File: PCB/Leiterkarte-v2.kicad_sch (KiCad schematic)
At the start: 50 parts

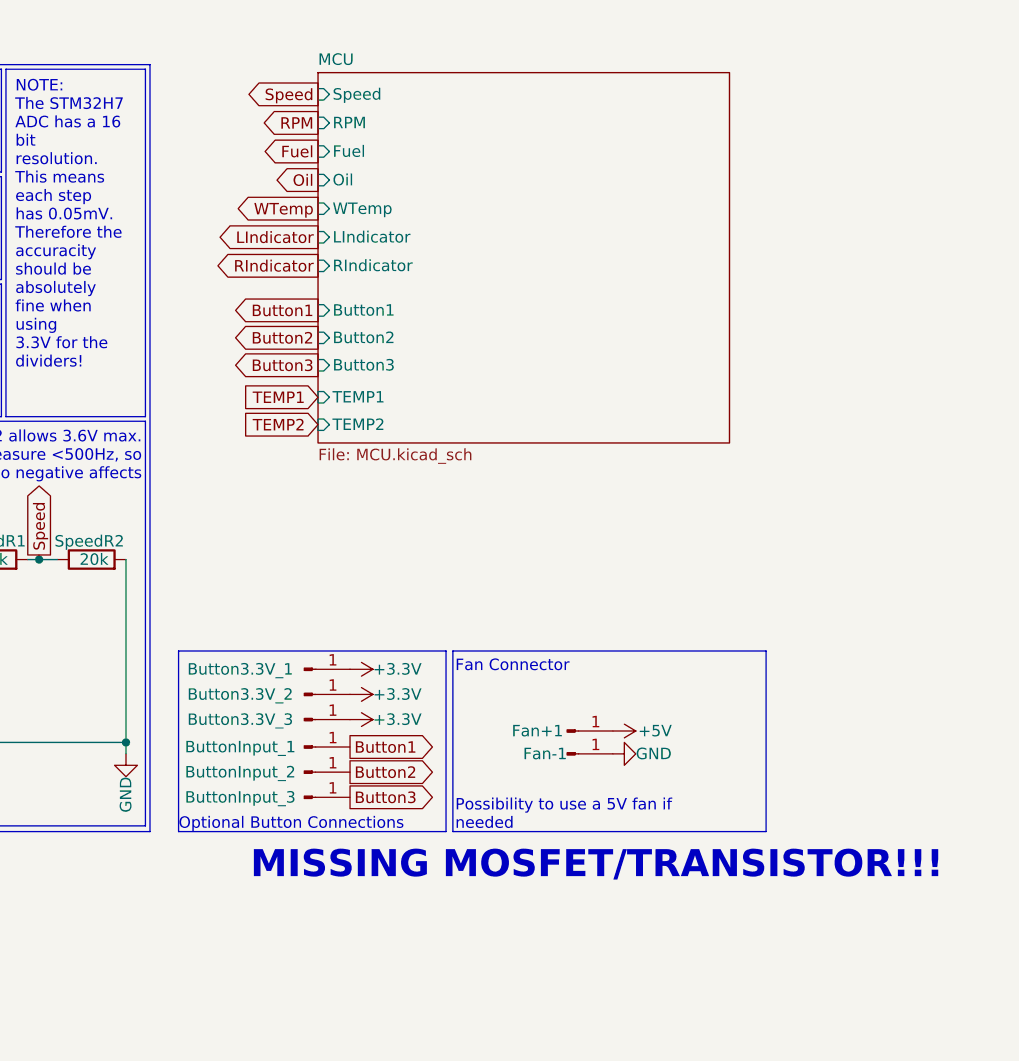
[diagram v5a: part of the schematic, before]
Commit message: Finalized circuit design; First try of PCB layout (FAILED)
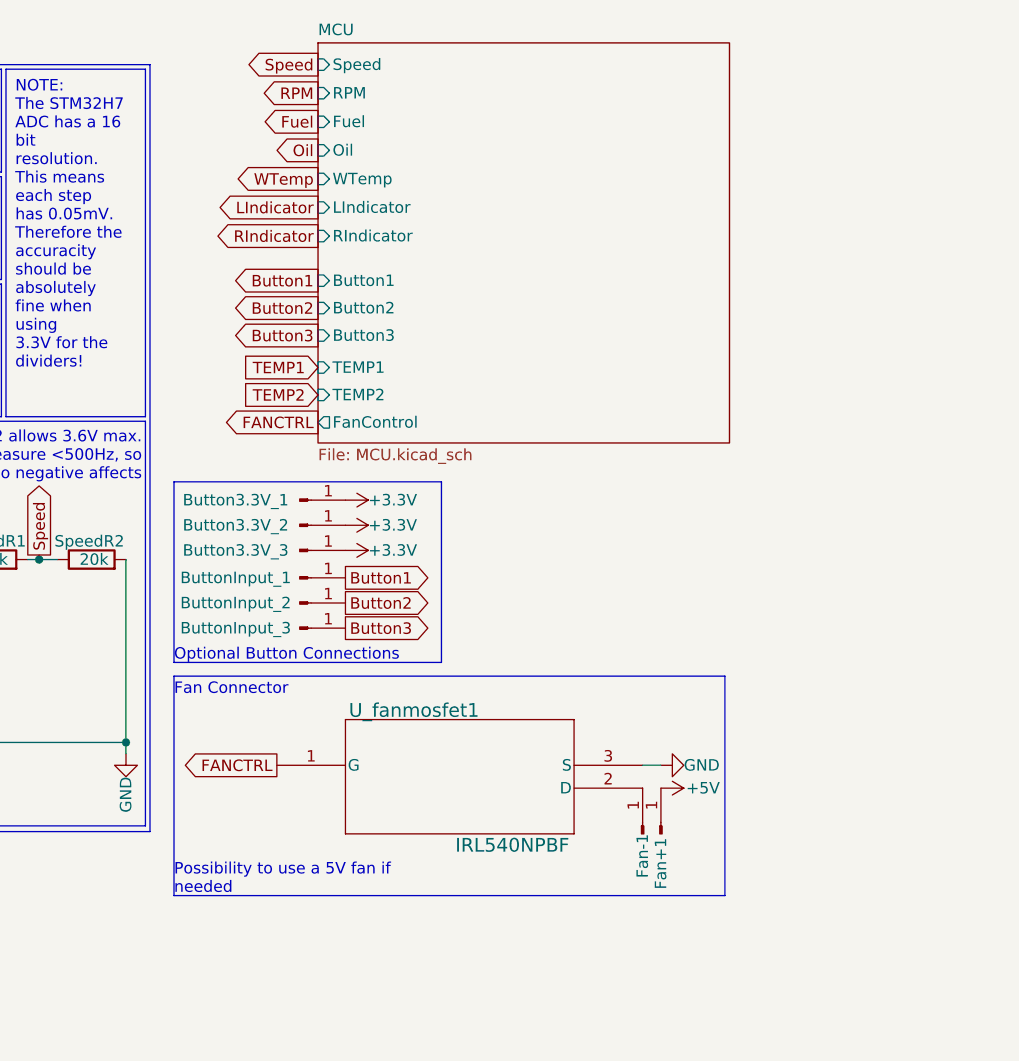
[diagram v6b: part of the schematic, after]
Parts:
- added U_fanmosfet1: IRL540NPBF, IRL540NPBF:PG-TO220-3_INF, symbol IRL540NPBF:IRL540NPBF
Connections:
- net GND: now also U_fanmosfet1.3 (S); no longer Fan-1.1 (Pin_1)
- new net: Fan-1.1 (Pin_1), U_fanmosfet1.2 (D)
- new net FANCTRL: U_fanmosfet1.1 (G)
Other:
- sheet MCU ports: added FanControl; removed none
- note removed: "MISSING MOSFET/TRANSISTOR!!!"
- moved on the sheet: Button3.3V_1, Button3.3V_2, Button3.3V_3, ButtonInput_1, ButtonInput_2, ButtonInput_3, Fan-1

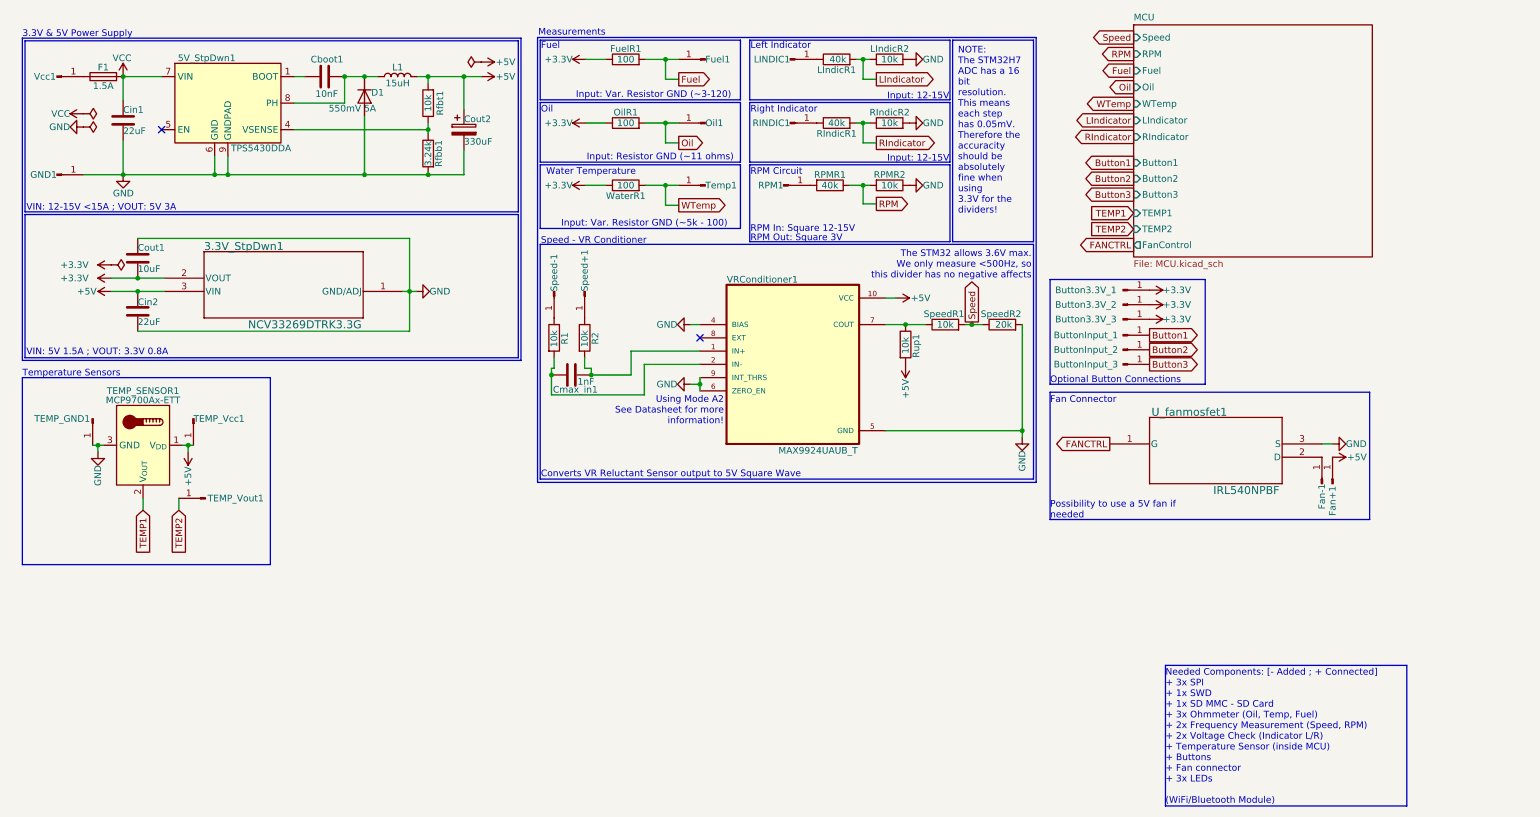
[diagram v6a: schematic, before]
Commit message: Finalized circuit design; Added PCB layout
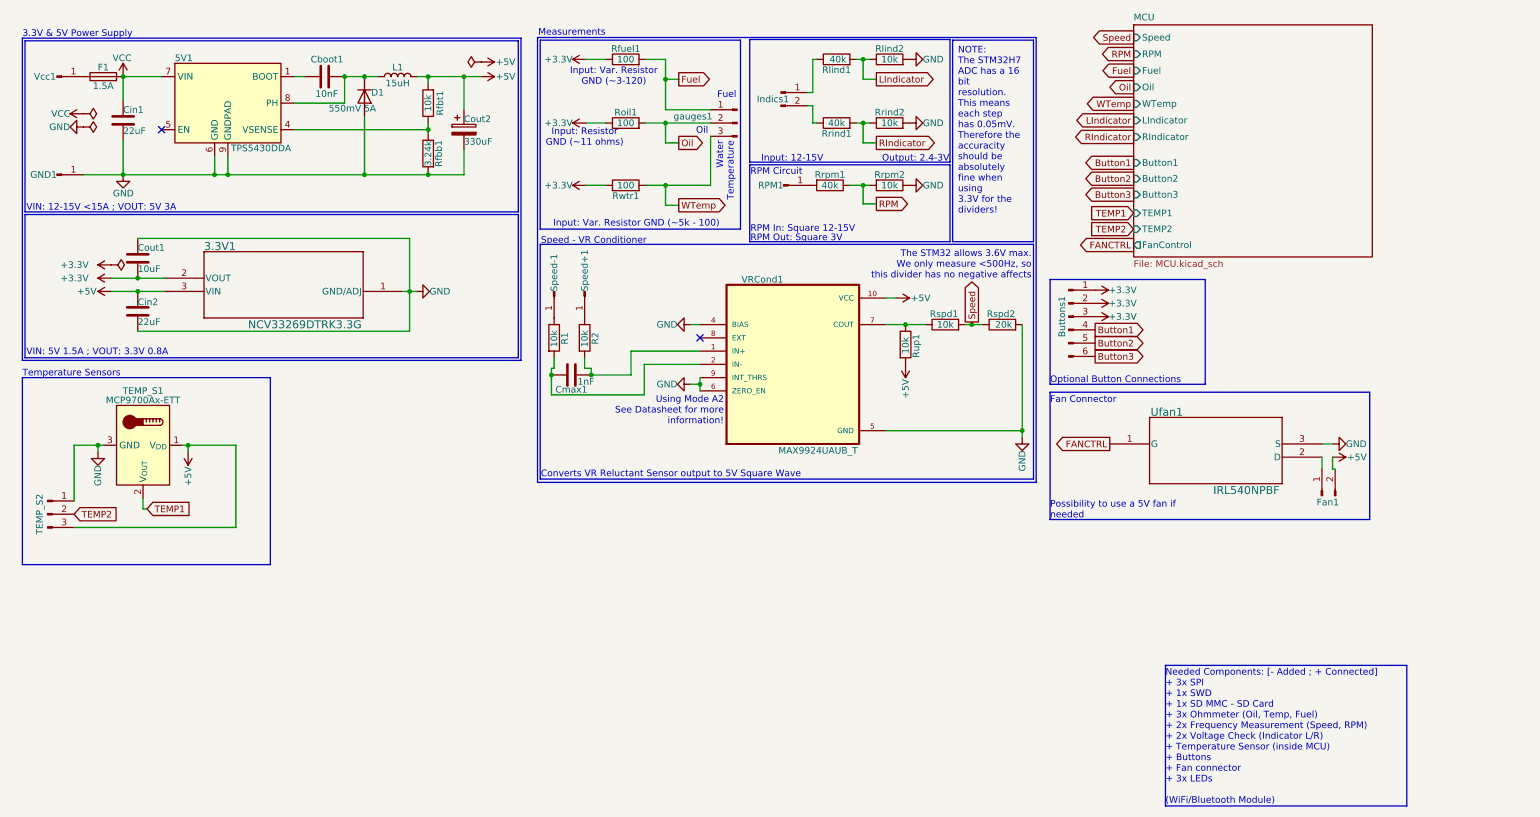
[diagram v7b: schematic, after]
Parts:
- removed Button3.3V_1, Button3.3V_2, Button3.3V_3, ButtonInput_1, ButtonInput_2, ButtonInput_3, Fan+1, Fan-1, Fuel1, LINDIC1, Oil1, RINDIC1, TEMP_GND1, TEMP_Vcc1, TEMP_Vout1, Temp1: Conn_01x01_Pin, Connector_PinHeader_2.54mm:PinHeader_1x01_P2.54mm_Vertical, symbol Connector:Conn_01x01_Pin
- added Buttons1: Conn_01x06_Pin, Connector_PinHeader_2.54mm:PinHeader_1x06_P2.54mm_Vertical, symbol Connector:Conn_01x06_Pin
- added Fan1, Indics1: Conn_01x02_Pin, Connector_JST:JST_SH_BM02B-SRSS-TB_1x02-1MP_P1.00mm_Vertical, symbol Connector:Conn_01x02_Pin
- added TEMP_S2, gauges1: Conn_01x03_Pin, Connector_JST:JST_SH_BM03B-SRSS-TB_1x03-1MP_P1.00mm_Vertical, symbol Connector:Conn_01x03_Pin
- renumbered 3.3V_StpDwn1 to 3.3V1, 5V_StpDwn1 to 5V1, Cmax_in1 to Cmax1, FuelR1 to Rfuel1, LIndicR1 to Rlind1, LIndicR2 to Rlind2, OilR1 to Roil1, RIndicR1 to Rrind1, RIndicR2 to Rrind2, RPMR1 to Rrpm1, RPMR2 to Rrpm2, SpeedR1 to Rspd1, SpeedR2 to Rspd2, WaterR1 to Rwtr1, TEMP_SENSOR1 to TEMP_S1, U_fanmosfet1 to Ufan1, VRConditioner1 to VRCond1
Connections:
- net +3.3V: now also Buttons1.1 (Pin_1), Buttons1.2 (Pin_2), Buttons1.3 (Pin_3)
- net +5V: now also Fan1.2 (Pin_2), TEMP_S2.3 (Pin_3)
- net Button1: now also Buttons1.4 (Pin_4)
- net Button2: now also Buttons1.5 (Pin_5)
- net Button3: now also Buttons1.6 (Pin_6)
- net Fuel: now also gauges1.1 (Pin_1)
- net GND: now also TEMP_S2.1 (Pin_1)
- net Oil: now also gauges1.2 (Pin_2)
- net TEMP2: now also TEMP_S2.2 (Pin_2)
- net WTemp: now also gauges1.3 (Pin_3)
- net at Rlind1.1: now also Indics1.1 (Pin_1)
- net at Rrind1.1: now also Indics1.2 (Pin_2)
- net at Ufan1.2 (D): now also Fan1.1 (Pin_1)
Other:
- note added: "Output: 2.4-3V"
- note removed: "Left Indicator"
- note removed: "Right Indicator"

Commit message: Replaced Inductor L1; Replaced MOSFET; Places some vias in the ground pours
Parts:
- removed Ufan1: IRL540NPBF, IRL540NPBF:PG-TO220-3_INF, symbol IRL540NPBF:IRL540NPBF
- added Qfan1: 2N7002-HXY, Package_TO_SOT_SMD:SOT-23, symbol Transistor_FET:2N7002
- L1: footprint Inductor_SMD:L_6.3x6.3_H3 -> FXL0630-1R5-M:INDM7066X300N
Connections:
- net FANCTRL: now also Qfan1.1 (G)
- net GND: now also Qfan1.2 (S)
- net at Fan1.1 (Pin_1): now also Qfan1.3 (D)
